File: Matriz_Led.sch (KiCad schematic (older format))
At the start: 22 parts, among them Q1 SMBT3904, Q2 SMBT3904, Q3 SMBT3904, Q4 SMBT3904, Q5 SMBT3904, U3 Matriz_5x7, U4 74HC595, U5 74HC595

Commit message: cambiados encoder y potenciometro
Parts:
- R1, R10, R11, R12, R2, R3, R4, R5, R6, R7, R8, R9: footprint Resistors_SMD:R_0805 -> Resistencias:R_0805
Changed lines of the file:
@@
 $EndComp
 $Comp
-L GND #PWR14
+L GND #PWR010
 U 1 1 5793BD55
 P 5700 5850
-F 0 "#PWR14" H 5700 5600 50  0001 C CNN
+F 0 "#PWR010" H 5700 5600 50  0001 C CNN
 F 1 "GND" H 5700 5700 50  0000 C CNN
 F 2 "" H 5700 5850 50  0000 C CNN
@@
 F 0 "R1" V 4980 1750 50  0000 C CNN
 F 1 "120" V 4900 1750 50  0000 C CNN
-F 2 "Resistors_SMD:R_0805" V 4830 1750 50  0001 C CNN
+F 2 "Resistencias:R_0805" V 4830 1750 50  0001 C CNN
 F 3 "" H 4900 1750 50  0000 C CNN
 F 4 "VISHAY" H 4550 1850 60  0001 C CNN "Fabricante"
@@
 $EndComp
 $Comp
-L GND #PWR13
+L GND #PWR011
 U 1 1 5793BDB6
 P 2350 4450
-F 0 "#PWR13" H 2350 4200 50  0001 C CNN
+F 0 "#PWR011" H 2350 4200 50  0001 C CNN
 F 1 "GND" H 2350 4300 50  0000 C CNN
 F 2 "" H 2350 4450 50  0000 C CNN
@@
 $EndComp
 $Comp
-L +5V #PWR12
+L +5V #PWR012
 U 1 1 5793BDC9
 P 2150 1600
-F 0 "#PWR12" H 2150 1450 50  0001 C CNN
+F 0 "#PWR012" H 2150 1450 50  0001 C CNN
 F 1 "+5V" H 2150 1740 50  0000 C CNN
 F 2 "" H 2150 1600 50  0000 C CNN
@@
 $EndComp
 $Comp
-L GND #PWR9
+L GND #PWR013
 U 1 1 5793BDCF
 P 1150 2350
-F 0 "#PWR9" H 1150 2100 50  0001 C CNN
+F 0 "#PWR013" H 1150 2100 50  0001 C CNN
 F 1 "GND" H 1150 2200 50  0000 C CNN
 F 2 "" H 1150 2350 50  0000 C CNN
@@
 $EndComp
 $Comp
-L +5V #PWR8
+L +5V #PWR014
 U 1 1 5793BDD5
 P 1150 1800
-F 0 "#PWR8" H 1150 1650 50  0001 C CNN
+F 0 "#PWR014" H 1150 1650 50  0001 C CNN
 F 1 "+5V" H 1150 1940 50  0000 C CNN
 F 2 "" H 1150 1800 50  0000 C CNN
@@
 F 0 "R2" V 4630 1850 50  0000 C CNN
 F 1 "120" V 4550 1850 50  0000 C CNN
-F 2 "Resistors_SMD:R_0805" V 4480 1850 50  0001 C CNN
+F 2 "Resistencias:R_0805" V 4480 1850 50  0001 C CNN
 F 3 "" H 4550 1850 50  0000 C CNN
 F 4 "VISHAY" H 4550 1850 60  0001 C CNN "Fabricante"
@@
 F 0 "R4" V 4630 2050 50  0000 C CNN
 F 1 "120" V 4550 2050 50  0000 C CNN
-F 2 "Resistors_SMD:R_0805" V 4480 2050 50  0001 C CNN
+F 2 "Resistencias:R_0805" V 4480 2050 50  0001 C CNN
 F 3 "" H 4550 2050 50  0000 C CNN
 F 4 "VISHAY" H 4550 1850 60  0001 C CNN "Fabricante"
@@
 F 0 "R6" V 4630 2250 50  0000 C CNN
 F 1 "120" V 4550 2250 50  0000 C CNN
-F 2 "Resistors_SMD:R_0805" V 4480 2250 50  0001 C CNN
+F 2 "Resistencias:R_0805" V 4480 2250 50  0001 C CNN
 F 3 "" H 4550 2250 50  0000 C CNN
 F 4 "VISHAY" H 4550 1850 60  0001 C CNN "Fabricante"
@@
 F 0 "R3" V 4980 1950 50  0000 C CNN
 F 1 "120" V 4900 1950 50  0000 C CNN
-F 2 "Resistors_SMD:R_0805" V 4830 1950 50  0001 C CNN
+F 2 "Resistencias:R_0805" V 4830 1950 50  0001 C CNN
 F 3 "" H 4900 1950 50  0000 C CNN
 F 4 "VISHAY" H 4550 1850 60  0001 C CNN "Fabricante"
@@
 F 0 "R5" V 4980 2150 50  0000 C CNN
 F 1 "120" V 4900 2150 50  0000 C CNN
-F 2 "Resistors_SMD:R_0805" V 4830 2150 50  0001 C CNN
+F 2 "Resistencias:R_0805" V 4830 2150 50  0001 C CNN
 F 3 "" H 4900 2150 50  0000 C CNN
 F 4 "VISHAY" H 4550 1850 60  0001 C CNN "Fabricante"
@@
 F 0 "R7" V 4980 2350 50  0000 C CNN
 F 1 "120" V 4900 2350 50  0000 C CNN
-F 2 "Resistors_SMD:R_0805" V 4830 2350 50  0001 C CNN
+F 2 "Resistencias:R_0805" V 4830 2350 50  0001 C CNN
 F 3 "" H 4900 2350 50  0000 C CNN
 F 4 "VISHAY" H 4550 1850 60  0001 C CNN "Fabricante"
@@
 F 0 "R8" V 4200 3550 50  0000 C CNN
 F 1 "1K" V 4300 3550 50  0000 C CNN
-F 2 "Resistors_SMD:R_0805" V 4230 3550 50  0001 C CNN
+F 2 "Resistencias:R_0805" V 4230 3550 50  0001 C CNN
 F 3 "" H 4300 3550 50  0000 C CNN
 F 4 "VISHAY" H 4300 3550 60  0001 C CNN "Fabricante"
@@
 F 0 "R9" V 4600 3950 50  0000 C CNN
 F 1 "1K" V 4700 3950 50  0000 C CNN
-F 2 "Resistors_SMD:R_0805" V 4630 3950 50  0001 C CNN
+F 2 "Resistencias:R_0805" V 4630 3950 50  0001 C CNN
 F 3 "" H 4700 3950 50  0000 C CNN
 F 4 "VISHAY" H 4300 3550 60  0001 C CNN "Fabricante"
@@
 F 0 "R10" V 5000 4350 50  0000 C CNN
 F 1 "1K" V 5100 4350 50  0000 C CNN
-F 2 "Resistors_SMD:R_0805" V 5030 4350 50  0001 C CNN
+F 2 "Resistencias:R_0805" V 5030 4350 50  0001 C CNN
 F 3 "" H 5100 4350 50  0000 C CNN
 F 4 "VISHAY" H 4300 3550 60  0001 C CNN "Fabricante"
@@
 F 0 "R11" V 5400 4750 50  0000 C CNN
 F 1 "1K" V 5500 4750 50  0000 C CNN
-F 2 "Resistors_SMD:R_0805" V 5430 4750 50  0001 C CNN
+F 2 "Resistencias:R_0805" V 5430 4750 50  0001 C CNN
 F 3 "" H 5500 4750 50  0000 C CNN
 F 4 "VISHAY" H 4300 3550 60  0001 C CNN "Fabricante"
@@
 F 0 "R12" V 5800 5150 50  0000 C CNN
 F 1 "1K" V 5900 5150 50  0000 C CNN
-F 2 "Resistors_SMD:R_0805" V 5830 5150 50  0001 C CNN
+F 2 "Resistencias:R_0805" V 5830 5150 50  0001 C CNN
 F 3 "" H 5900 5150 50  0000 C CNN
 F 4 "VISHAY" H 4300 3550 60  0001 C CNN "Fabricante"
@@
 $EndComp
 $Comp
-L GND #PWR11
+L GND #PWR015
 U 1 1 5793BEDF
 P 1150 4150
-F 0 "#PWR11" H 1150 3900 50  0001 C CNN
+F 0 "#PWR015" H 1150 3900 50  0001 C CNN
 F 1 "GND" H 1150 4000 50  0000 C CNN
 F 2 "" H 1150 4150 50  0000 C CNN
@@
 $EndComp
 $Comp
-L +5V #PWR10
+L +5V #PWR016
 U 1 1 5793BEE5
 P 1150 3600
-F 0 "#PWR10" H 1150 3450 50  0001 C CNN
+F 0 "#PWR016" H 1150 3450 50  0001 C CNN
 F 1 "+5V" H 1150 3740 50  0000 C CNN
 F 2 "" H 1150 3600 50  0000 C CNN
@@
 30 0C C3 30 0C C3 30 0C C3 30 3E 7B 4C E0 30 0C C3 30 0C C3 30 0C C3 30 0C E3 B3 C7 04 0E C3 30
 0C C3 30 0C C3 30 0C C3 30 3E 7B 4C E0 30 0C C3 30 0C C3 30 0C C3 30 0C E3 B3 E7 DF 01 18 4D 27
-06 D5 63 A7 50 00 00 00 00 49 45 4E 44 AE 42 60 82 87
+06 D5 63 A7 50 00 00 00 00 49 45 4E 44 AE 42 60 82 4E
 EndData
 $EndBitmap

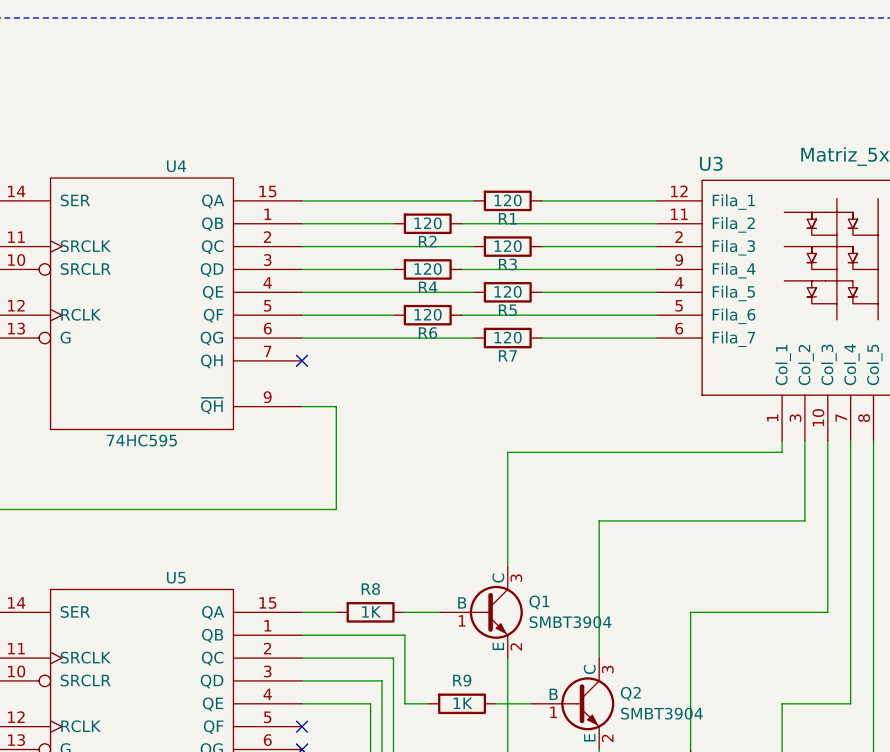
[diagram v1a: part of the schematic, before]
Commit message: añadidos driver para led y conectores para fotodiodos infrarrojos
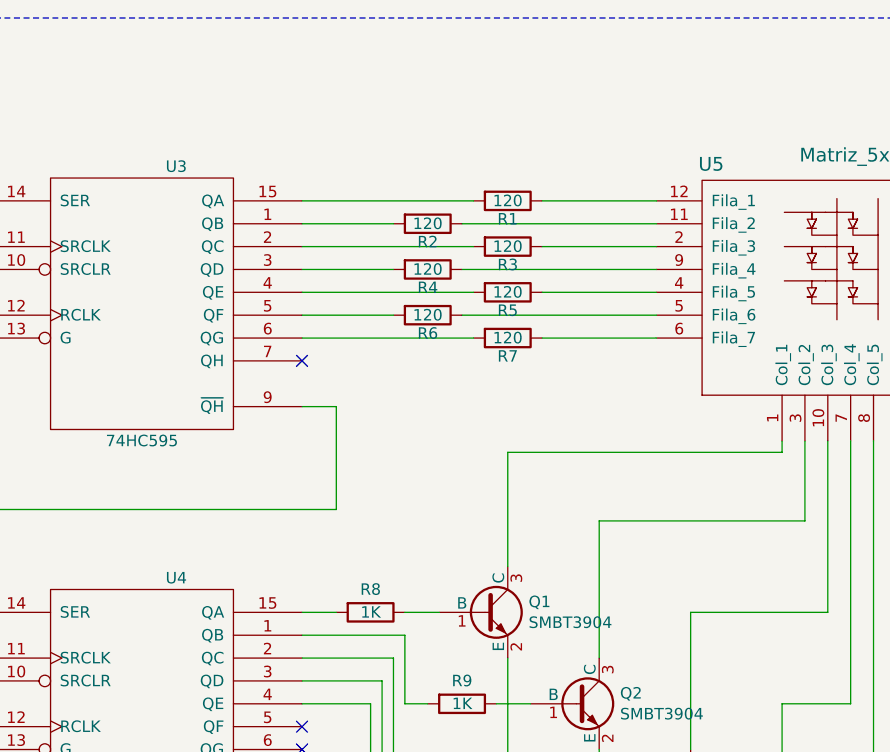
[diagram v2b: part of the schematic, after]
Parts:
- renumbered U4 to U3, U5 to U4, U3 to U5
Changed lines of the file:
@@
 EESchema Schematic File Version 2
+LIBS:Interfaces
+LIBS:Nano_PB-rescue
 LIBS:Sensores
 LIBS:power
@@
 LIBS:valves
 LIBS:MyLibrary
+LIBS:matriz_led
 LIBS:Nano_PB-cache
-EELAYER 25 0
+EELAYER 26 0
 EELAYER END
 $Descr A4 11693 8268
 encoding utf-8
-Sheet 4 15
+Sheet 4 16
 Title "Matriz de LED's"
-Date "2016-08-07"
-Rev "V.0.2"
+Date "2017-01-04"
+Rev "V.0.3"
 Comp "NanoPlayBoard"
 Comment1 "Creada por Antonio Morales"
@@
 $EndDescr
 $Comp
-L Matriz_5x7_Anodo_Filas U3
+L Matriz_5x7_Anodo_Filas U5
 U 1 1 5793BD4E
 P 6100 2800
-F 0 "U3" H 5790 4010 60  0000 C CNN
+F 0 "U5" H 5790 4010 60  0000 C CNN
 F 1 "Matriz_5x7" H 6400 4050 60  0000 C CNN
 F 2 "Leds:Matriz_Led_7X5" H 6190 3940 60  0001 C CNN
@@
 $EndComp
 $Comp
-L GND #PWR010
+L GND #PWR012
 U 1 1 5793BD55
 P 5700 5850
-F 0 "#PWR010" H 5700 5600 50  0001 C CNN
+F 0 "#PWR012" H 5700 5600 50  0001 C CNN
 F 1 "GND" H 5700 5700 50  0000 C CNN
 F 2 "" H 5700 5850 50  0000 C CNN
@@
 $EndComp
 $Comp
-L 74HC595 U4
+L 74HC595 U3
 U 1 1 5793BDAF
 P 3300 2200
-F 0 "U4" H 3450 2800 50  0000 C CNN
+F 0 "U3" H 3450 2800 50  0000 C CNN
 F 1 "74HC595" H 3300 1600 50  0000 C CNN
 F 2 "Housings_SOIC:SOIC-16_3.9x9.9mm_Pitch1.27mm" H 3300 2200 50  0001 C CNN
@@
 $EndComp
 $Comp
-L GND #PWR011
+L GND #PWR013
 U 1 1 5793BDB6
 P 2350 4450
-F 0 "#PWR011" H 2350 4200 50  0001 C CNN
+F 0 "#PWR013" H 2350 4200 50  0001 C CNN
 F 1 "GND" H 2350 4300 50  0000 C CNN
 F 2 "" H 2350 4450 50  0000 C CNN
@@
 $EndComp
 $Comp
-L +5V #PWR012
+L +5V #PWR014
 U 1 1 5793BDC9
 P 2150 1600
-F 0 "#PWR012" H 2150 1450 50  0001 C CNN
+F 0 "#PWR014" H 2150 1450 50  0001 C CNN
 F 1 "+5V" H 2150 1740 50  0000 C CNN
 F 2 "" H 2150 1600 50  0000 C CNN
@@
 $EndComp
 $Comp
-L GND #PWR013
+L GND #PWR015
 U 1 1 5793BDCF
 P 1150 2350
-F 0 "#PWR013" H 1150 2100 50  0001 C CNN
+F 0 "#PWR015" H 1150 2100 50  0001 C CNN
 F 1 "GND" H 1150 2200 50  0000 C CNN
 F 2 "" H 1150 2350 50  0000 C CNN
@@
 $EndComp
 $Comp
-L +5V #PWR014
+L +5V #PWR016
 U 1 1 5793BDD5
 P 1150 1800
-F 0 "#PWR014" H 1150 1650 50  0001 C CNN
+F 0 "#PWR016" H 1150 1650 50  0001 C CNN
 F 1 "+5V" H 1150 1940 50  0000 C CNN
 F 2 "" H 1150 1800 50  0000 C CNN
@@
 MATRIZ DE LEDS 5x7
 $Comp
-L 74HC595 U5
+L 74HC595 U4
 U 1 1 5793BEAB
 P 3300 4000
-F 0 "U5" H 3450 4600 50  0000 C CNN
+F 0 "U4" H 3450 4600 50  0000 C CNN
 F 1 "74HC595" H 3300 3400 50  0000 C CNN
 F 2 "Housings_SOIC:SOIC-16_3.9x9.9mm_Pitch1.27mm" H 3300 4000 50  0001 C CNN
@@
 $EndComp
 $Comp
-L GND #PWR015
+L GND #PWR017
 U 1 1 5793BEDF
 P 1150 4150
-F 0 "#PWR015" H 1150 3900 50  0001 C CNN
+F 0 "#PWR017" H 1150 3900 50  0001 C CNN
 F 1 "GND" H 1150 4000 50  0000 C CNN
 F 2 "" H 1150 4150 50  0000 C CNN
@@
 $EndComp
 $Comp
-L +5V #PWR016
+L +5V #PWR018
 U 1 1 5793BEE5
 P 1150 3600
-F 0 "#PWR016" H 1150 3450 50  0001 C CNN
+F 0 "#PWR018" H 1150 3450 50  0001 C CNN
 F 1 "+5V" H 1150 3740 50  0000 C CNN
 F 2 "" H 1150 3600 50  0000 C CNN
@@
 30 0C C3 30 0C C3 30 0C C3 30 3E 7B 4C E0 30 0C C3 30 0C C3 30 0C C3 30 0C E3 B3 C7 04 0E C3 30
 0C C3 30 0C C3 30 0C C3 30 3E 7B 4C E0 30 0C C3 30 0C C3 30 0C C3 30 0C E3 B3 E7 DF 01 18 4D 27
-06 D5 63 A7 50 00 00 00 00 49 45 4E 44 AE 42 60 82 4E
+06 D5 63 A7 50 00 00 00 00 49 45 4E 44 AE 42 60 82
 EndData
 $EndBitmap
@@
 50 17 92 01 51 92 64 0C CE 27 7B 4E 87 A3 FC C9 E9 39 BC D0 3B DC 1F CF E6 3C 60 30 83 10 3D 18
 F4 0B 89 52 73 00 8B 80 91 08 28 22 8F 6D AB AA BD D3 E7 C4 3E A7 59 B4 A9 94 4D 1C A1 84 52 AC
-9A 46 F6 7A E1 FF 00 F0 A4 0C 74 26 CB 7B D1 00 00 00 00 49 45 4E 44 AE 42 60 82 00
+9A 46 F6 7A E1 FF 00 F0 A4 0C 74 26 CB 7B D1 00 00 00 00 49 45 4E 44 AE 42 60 82
 EndData
 $EndBitmap

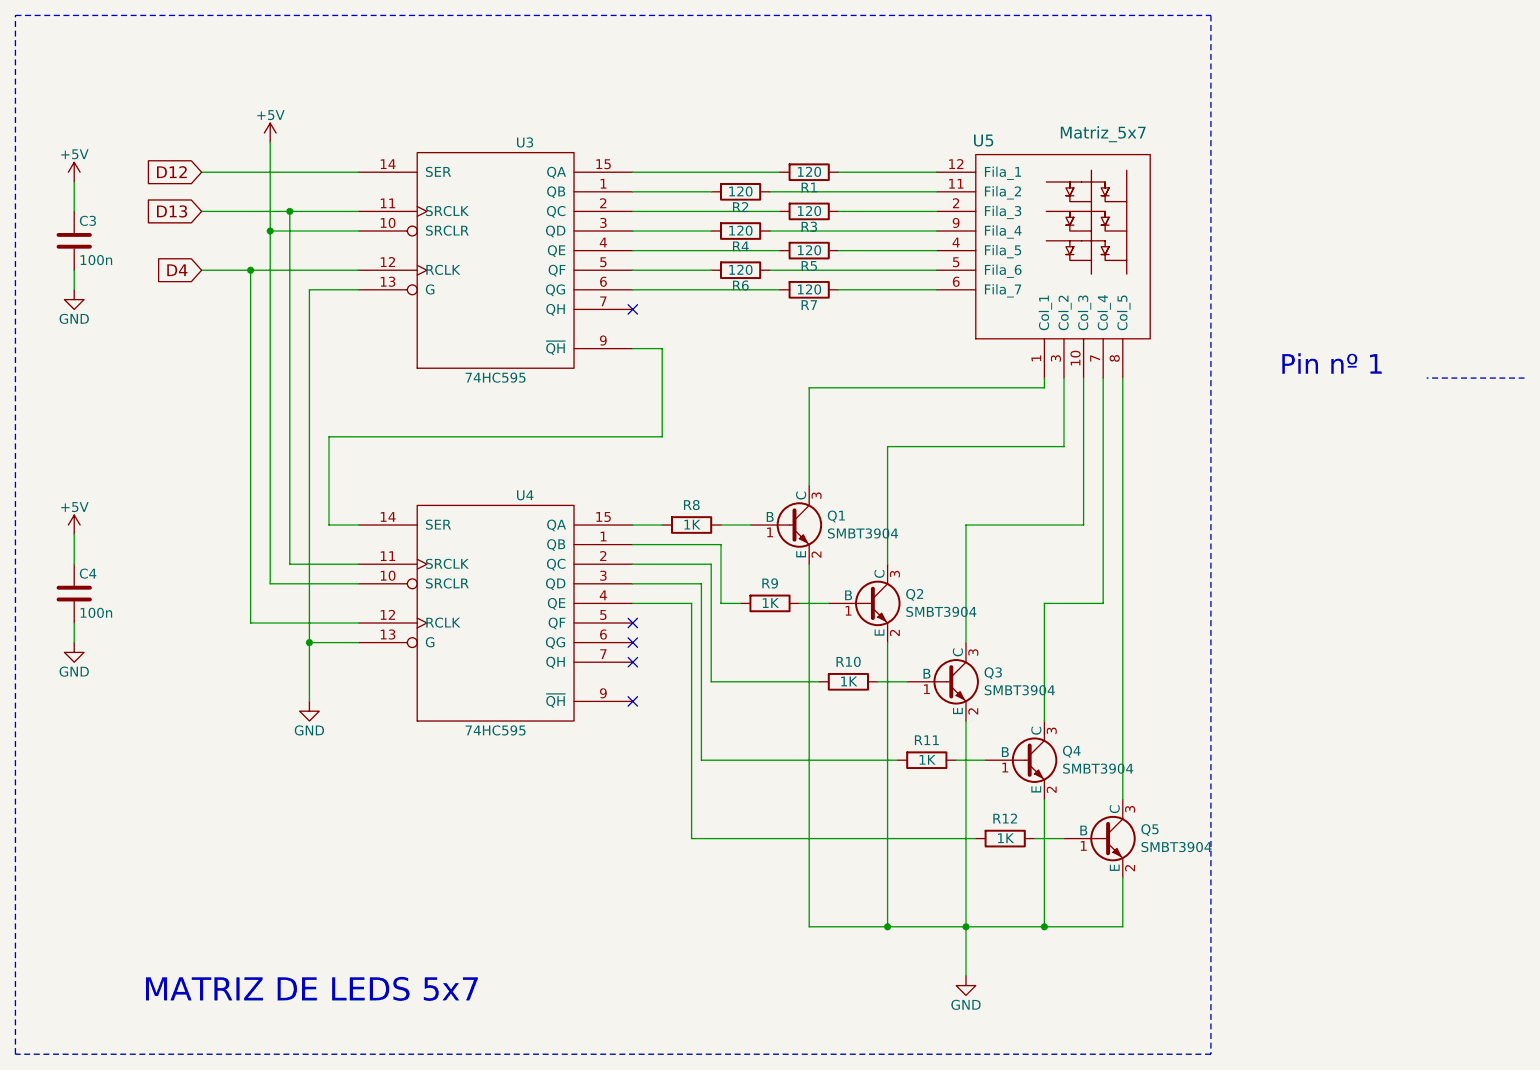
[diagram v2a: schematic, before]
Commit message: Se añade un expansor GPIO al esquema y se elminan registros y codificador
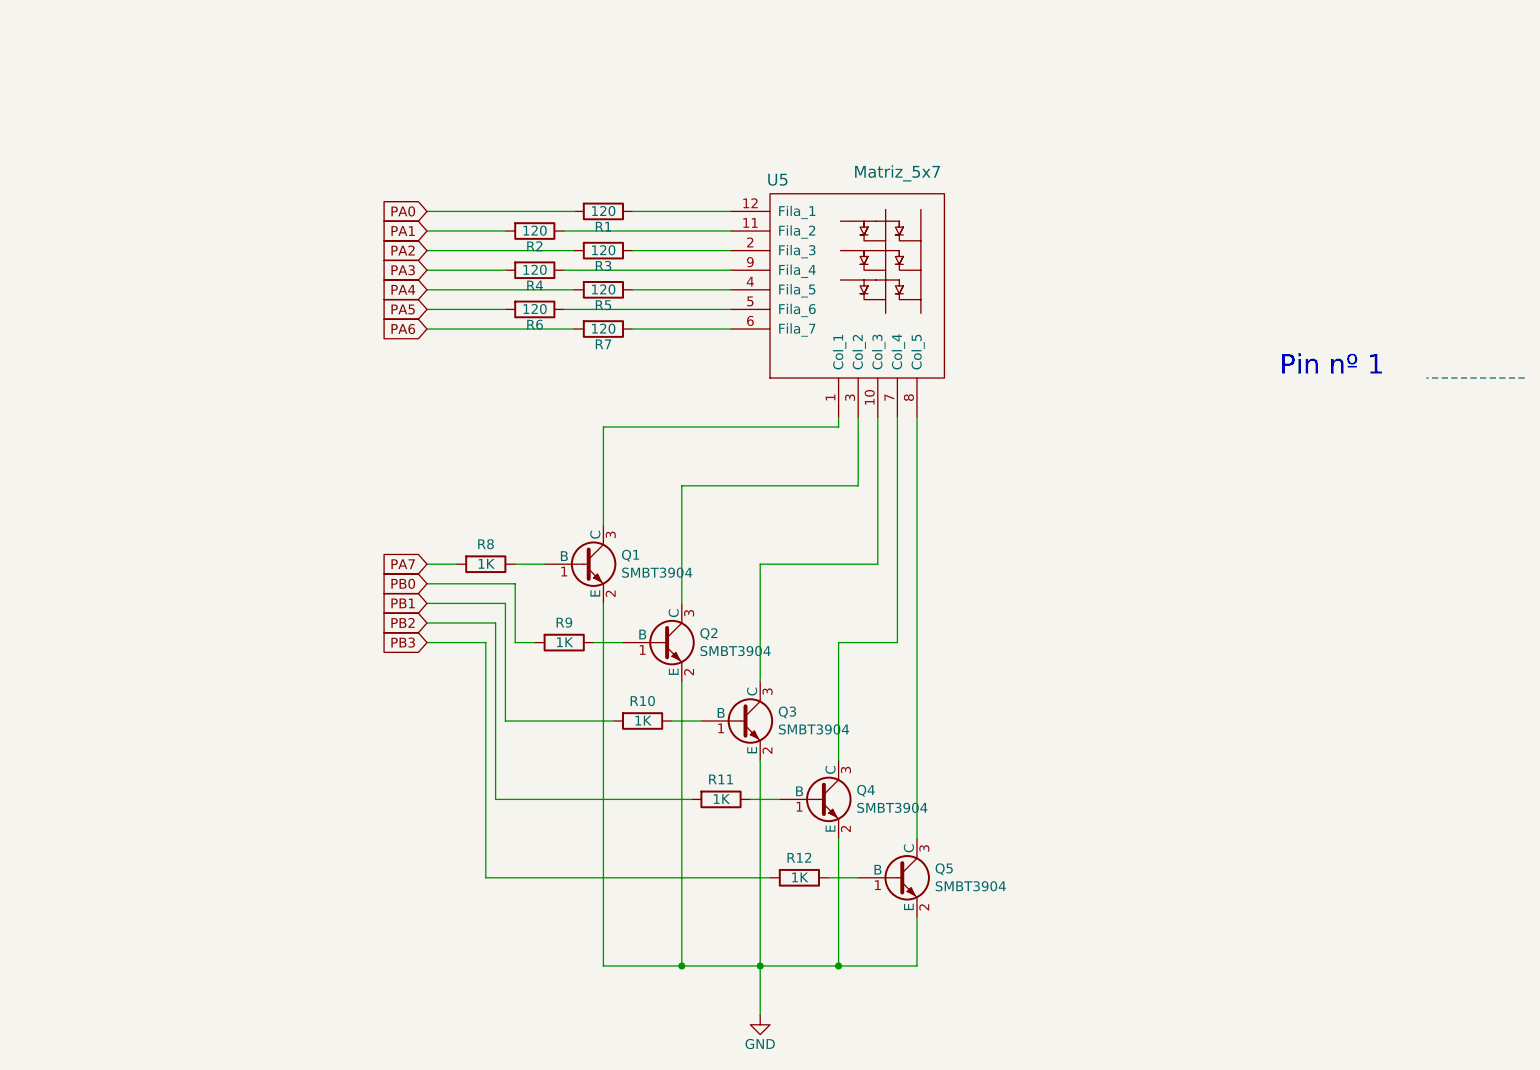
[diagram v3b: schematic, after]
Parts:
- removed C3, C4: 100n, Capacitors_SMD:C_0805, symbol C
- removed U3, U4: 74HC595, Housings_SOIC:SOIC-16_3.9x9.9mm_Pitch1.27mm, symbol 74HC595
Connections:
- net PA0: now reaches R1.2
- net PA1: now reaches R2.2
- net PA2: now reaches R3.2
- net PA3: now reaches R4.2
- net PA4: now reaches R5.2
- net PA5: now reaches R6.2
- net PA6: now reaches R7.2
- net PA7: now reaches R8.2
- net PB0: now reaches R9.2
- net PB1: now reaches R10.2
- net PB2: now reaches R11.2
- net PB3: now reaches R12.2
- no-connect marks 5 -> 0
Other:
- note removed: "MATRIZ DE LEDS 5x7"
- moved on the sheet: Q1, Q2, Q3, Q4, Q5, R1, R10, R11, R12, R2, R3, R4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

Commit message: finalizado enrutado provisional
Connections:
- net PB0 renamed PB4
- net PB1 renamed PB5
- net PB2 renamed PB6
- net PB3 renamed PB7
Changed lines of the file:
@@
 PA7
 Text GLabel 2950 3850 0    50   Input ~ 0
-PB0
+PB4
 Text GLabel 2950 3950 0    50   Input ~ 0
-PB1
+PB5
 Text GLabel 2950 4050 0    50   Input ~ 0
-PB2
+PB6
 Text GLabel 2950 4150 0    50   Input ~ 0
-PB3
+PB7
 $EndSCHEMATC
